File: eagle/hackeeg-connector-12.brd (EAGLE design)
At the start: 114.6 x 27.9 mm, 21 parts

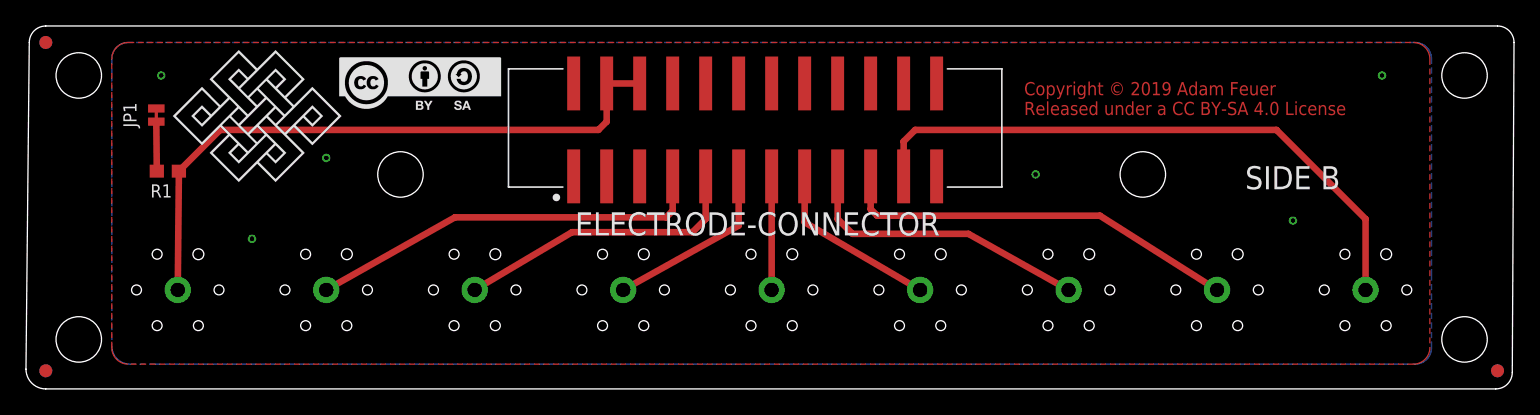
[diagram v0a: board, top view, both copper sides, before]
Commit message: added connector, finished schematic and routed
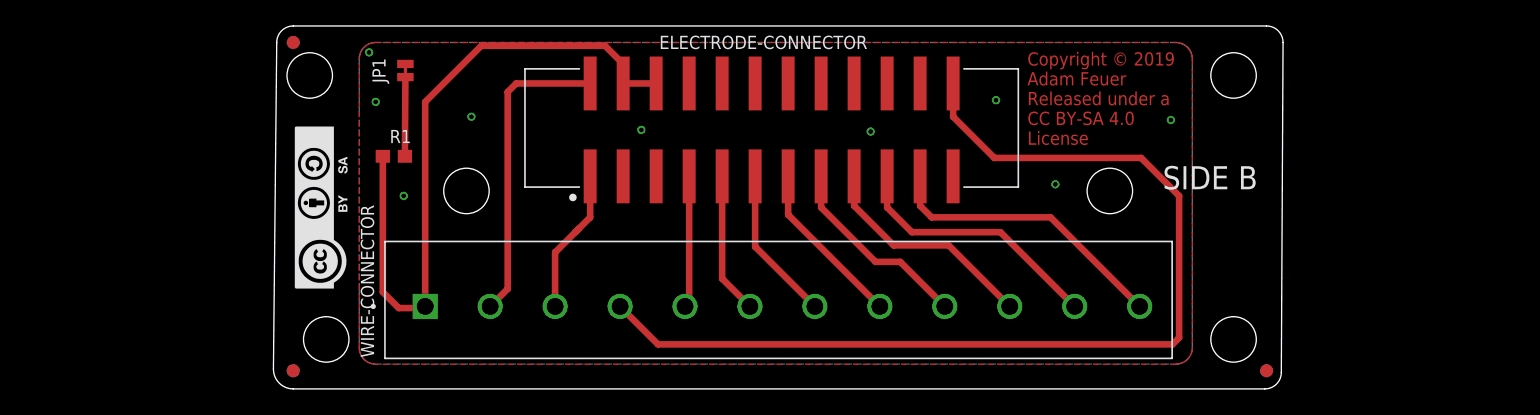
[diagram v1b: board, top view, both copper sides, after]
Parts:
- removed AGND, IN1P, IN2P, IN3P, IN4P, IN5P, IN6P, IN7P, IN8P: PO37729HEX-110, po-37729:HEX-110
- added WIRE-CONNECTOR: OSTTA120161B, OSTTA120161B:ONSHORE_OSTTA120161B
- moved JP1 19.5 mm to (29.0, 27.1)
- moved FD1 19.1 mm to (20.3, 3.94)
- moved FD2 19.1 mm to (20.3, 29.2)
- moved FD5 19.1 mm to (20.3, 29.2)
- moved FD6 19.1 mm to (20.3, 3.94)
- moved FD3 17.8 mm to (95.2, 3.94)
- moved FD4 17.8 mm to (95.2, 3.94)
- moved R1 17.4 mm to (28.1, 20.4), turned to 0 degrees
- moved U$13 13.6 mm to (24.8, 10.2), turned to 90 degrees
- moved U$1 12.4 mm to (30.1, 23.7), flipped to the bottom
- moved FRAME1 2.54 mm to (24.1, -10.2)
- moved ELECTRODE-CONNECTOR 1.27 mm to (57.1, 22.5)
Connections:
- removed net N$2: ELECTRODE-CONNECTOR.7, IN1P.SIGNAL
- removed net N$3: ELECTRODE-CONNECTOR.9, IN2P.SIGNAL
- removed net N$4: ELECTRODE-CONNECTOR.11, IN3P.SIGNAL
- removed net N$5: ELECTRODE-CONNECTOR.13, IN4P.SIGNAL
- removed net N$6: ELECTRODE-CONNECTOR.15, IN5P.SIGNAL
- removed net N$7: ELECTRODE-CONNECTOR.17, IN6P.SIGNAL
- removed net N$8: ELECTRODE-CONNECTOR.19, IN7P.SIGNAL
- removed net N$9: ELECTRODE-CONNECTOR.21, IN8P.SIGNAL
- new net AVDD: ELECTRODE-CONNECTOR.2, WIRE-CONNECTOR.2
- new net BIAS_ELEC: ELECTRODE-CONNECTOR.24, WIRE-CONNECTOR.4
- new net DVDD: ELECTRODE-CONNECTOR.1, WIRE-CONNECTOR.3
- new net IN1P: ELECTRODE-CONNECTOR.7, WIRE-CONNECTOR.5
- new net IN2P: ELECTRODE-CONNECTOR.9, WIRE-CONNECTOR.6
- new net IN3P: ELECTRODE-CONNECTOR.11, WIRE-CONNECTOR.7
- new net IN4P: ELECTRODE-CONNECTOR.13, WIRE-CONNECTOR.8
- new net IN5P: ELECTRODE-CONNECTOR.15, WIRE-CONNECTOR.9
- new net IN6P: ELECTRODE-CONNECTOR.17, WIRE-CONNECTOR.10
- new net IN7P: ELECTRODE-CONNECTOR.19, WIRE-CONNECTOR.11
- new net IN8P: ELECTRODE-CONNECTOR.21, WIRE-CONNECTOR.12
- net AGND1: now also WIRE-CONNECTOR.1; no longer AGND.SIGNAL
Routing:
- net BIAS_ELEC: track 0.00 -> 77.9 mm
- net N$9: track 46.9 -> 0.00 mm
- net N$8: track 31.1 -> 0.00 mm
- net N$2: track 31.0 -> 0.00 mm
- net AVDD: track 0.00 -> 23.7 mm
- net N$3: track 22.7 -> 0.00 mm
- net N$7: track 22.7 -> 0.00 mm
- net IN8P: track 0.00 -> 22.4 mm
- net IN7P: track 0.00 -> 20.0 mm
- net IN6P: track 0.00 -> 17.5 mm
- net IN5P: track 0.00 -> 15.1 mm
- net N$4: track 14.0 -> 0.00 mm
- net N$6: track 13.8 -> 0.00 mm
- net IN4P: track 0.00 -> 12.9 mm
- net IN3P: track 0.00 -> 11.9 mm
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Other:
- board size 114.6 x 27.9 mm -> 77.7 x 27.9 mm

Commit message: put wire connector on bottom of board
- labeled wire connector pins
- board is routed
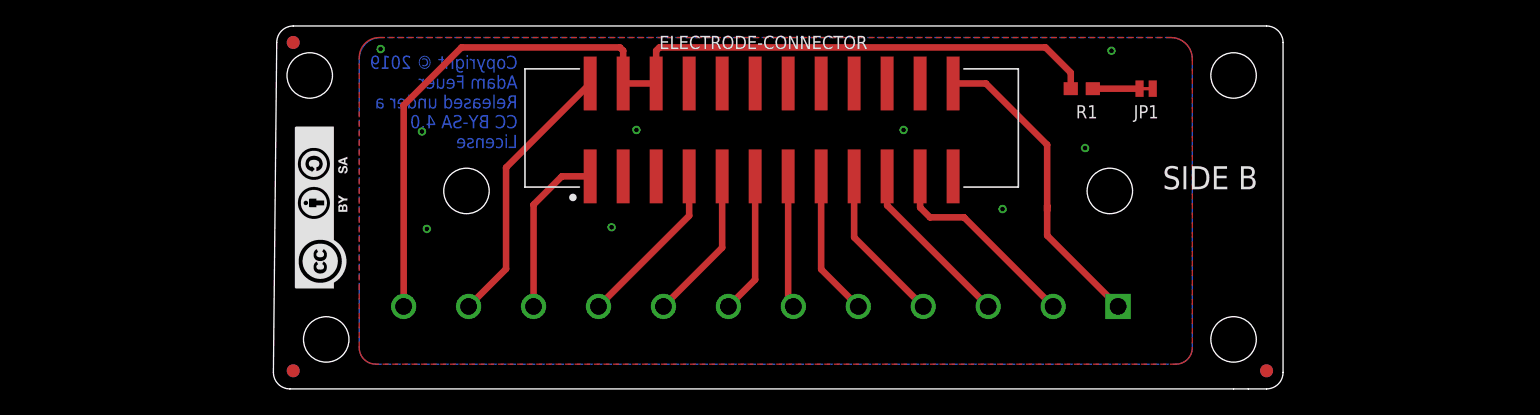
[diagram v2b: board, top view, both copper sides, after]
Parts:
- moved JP1 57.0 mm to (86.0, 25.7), turned to 0 degrees
- moved WIRE-CONNECTOR 53.3 mm to (83.8, 8.89), flipped to the bottom
- moved R1 53.2 mm to (81.0, 25.7)
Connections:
- net AGND1: now also WIRE-CONNECTOR.12; no longer WIRE-CONNECTOR.1
- net AVDD: now also WIRE-CONNECTOR.11; no longer WIRE-CONNECTOR.2
- net BIAS_ELEC: now also WIRE-CONNECTOR.1; no longer WIRE-CONNECTOR.4
- net DVDD: now also WIRE-CONNECTOR.10; no longer WIRE-CONNECTOR.3
- net IN1P: now also WIRE-CONNECTOR.9; no longer WIRE-CONNECTOR.5
- net IN2P: now also WIRE-CONNECTOR.8; no longer WIRE-CONNECTOR.6
- net IN4P: now also WIRE-CONNECTOR.6; no longer WIRE-CONNECTOR.8
- net IN5P: now also WIRE-CONNECTOR.5; no longer WIRE-CONNECTOR.9
- net IN6P: now also WIRE-CONNECTOR.4; no longer WIRE-CONNECTOR.10
- net IN7P: now also WIRE-CONNECTOR.3; no longer WIRE-CONNECTOR.11
- net IN8P: now also WIRE-CONNECTOR.2; no longer WIRE-CONNECTOR.12
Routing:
- net BIAS_ELEC: track 77.9 -> 24.3 mm
- net AGND1: track 53.2 -> 79.0 mm
- net IN7P: track 20.0 -> 13.2 mm
- net IN8P: track 22.4 -> 15.8 mm
- net IN6P: track 17.5 -> 12.2 mm
- net IN5P: track 15.1 -> 11.2 mm
- net DVDD: track 11.5 -> 14.8 mm
- net IN4P: track 12.9 -> 10.2 mm
- net IN1P: track 10.1 -> 12.9 mm
- net AVDD: track 23.7 -> 21.0 mm
- net N$17: track 6.10 -> 3.59 mm
- net IN3P: track 11.9 -> 10.9 mm
- net IN2P: track 10.9 -> 11.9 mm
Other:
- outline, holes or cut-outs redrawn
- board text added: "AGND"
- board text added: "AVDD"
- board text added: "BIAS"
- board text added: "DVDD"
- board text added: "IN1P"
- board text added: "IN2P"
- board text added: "IN3P"
- board text added: "IN4P"
- board text added: "IN5P"
- board text added: "IN6P"
- board text added: "IN7P"
- board text added: "IN8P"
